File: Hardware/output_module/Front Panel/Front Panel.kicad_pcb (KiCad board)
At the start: 2 copper layers, 50.8 x 130.2 mm, 21 parts

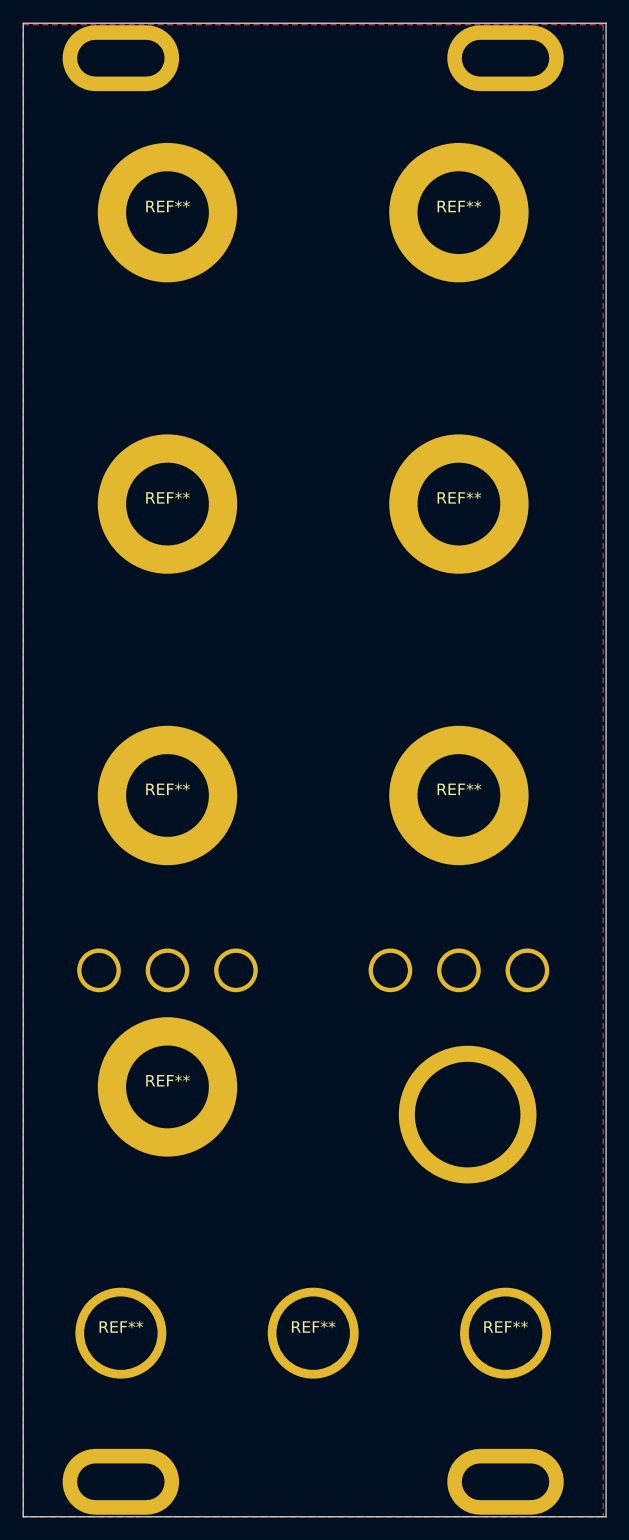
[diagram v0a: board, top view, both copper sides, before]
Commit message: update output module production mistakes
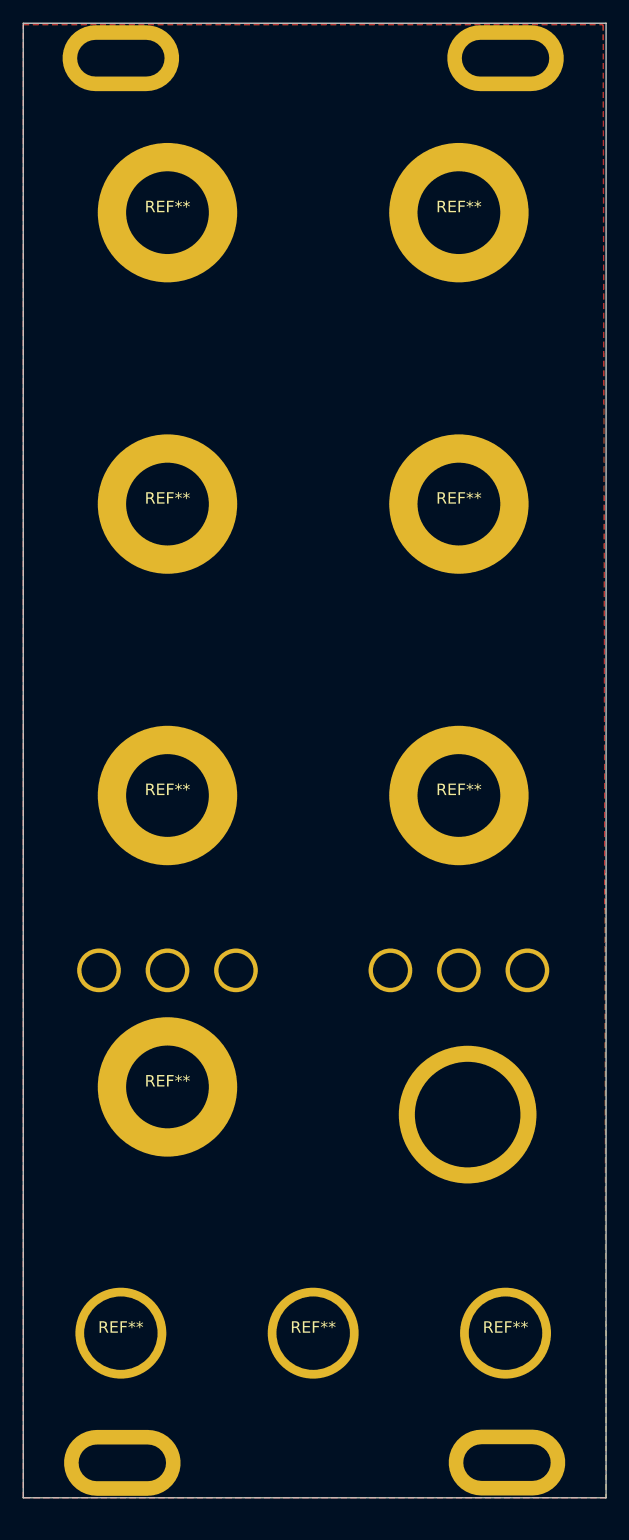
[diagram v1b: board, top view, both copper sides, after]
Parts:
- moved REF** 1.68 mm to (132.6, 158.6)
- moved REF** 1.66 mm to (99.1, 158.6)
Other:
- board size 50.8 x 130.2 mm -> 50.8 x 128.5 mm
- board text added: "Revision History Rev 1: Initial Proto Order Rev 2: Corrected Panel Height"
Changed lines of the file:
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@@
 	)
 	(paper "A4")
+	(title_block
+		(rev "2")
+	)
 	(layers
 		(0 "F.Cu" signal)
@@
 			(outputformat 1)
 			(mirror no)
-			(drillshape 1)
+			(drillshape 0)
 			(scaleselection 1)
-			(outputdirectory "")
+			(outputdirectory "rev 2/")
 		)
 	)
@@
 	(footprint "synthesis:PANEL_MOUNTING_HOLE"
 		(layer "F.Cu")
-		(at 132.461 160.274)
+		(at 132.588 158.5976)
 		(property "Reference" "REF**"
 			(at 0 -0.5 0)
@@
 	(footprint "synthesis:PANEL_MOUNTING_HOLE"
 		(layer "F.Cu")
-		(at 98.933 160.274)
+		(at 99.06 158.623)
 		(property "Reference" "REF**"
 			(at 0 -0.5 0)
@@
 	(gr_rect
 		(start 90.424 33.147)
-		(end 141.224 163.322)
+		(end 141.224 161.671)
 		(stroke
 			(width 0.05)
@@
 	)
 	(gr_text "OUTPUT\nMODULE"
-		(at 115.697 159.512 0)
+		(at 115.7224 158.2166 0)
 		(layer "F.Mask")
 		(effects
@@
 				(thickness 0.254)
 			)
+		)
+	)
+	(gr_text "Revision History\nRev 1: Initial Proto Order\nRev 2: Corrected Panel Height"
+		(at 229.6922 131.9276 0)
+		(layer "User.1")
+		(effects
+			(font
+				(size 1 1)
+				(thickness 0.15)
+			)
+			(justify left bottom)
 		)
 	)
@@
 		(polygon
 			(pts
-				(xy 90.424 33.274) (xy 140.97 33.274) (xy 140.97 163.322) (xy 90.424 163.322)
-			)
-		)
+				(xy 90.424 33.274) (xy 140.97 33.274) (xy 141.224 161.671) (xy 90.424 161.671)
+			)
+		)
